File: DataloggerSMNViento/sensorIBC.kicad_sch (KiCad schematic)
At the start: 2 parts

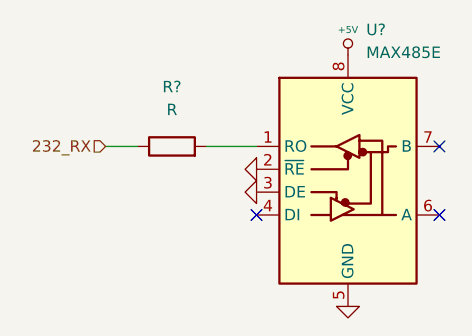
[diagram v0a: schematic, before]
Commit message: Agrego modificaciones al poncho de la EDU CIAA, también agrego una simulacion del circuito para tomar la tensión del ADC del tunnel
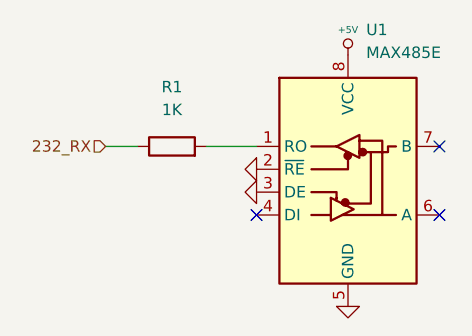
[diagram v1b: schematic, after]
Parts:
- R1: renamed from R?; value R -> 1K; footprint (none) -> Resistor_THT:R_Axial_DIN0207_L6.3mm_D2.5mm_P15.24mm_Horizontal
- U1: renamed from U?; footprint (none) -> Modulos:Rs485toTTL
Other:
- company: (none) -> Servicio Meteorológico Nacional - FIUBA - UBA
- title: (none) -> Datalogger para SCTV
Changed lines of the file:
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@@
 (kicad_sch (version 20211123) (generator eeschema)
   (paper "A4")
+  (title_block
+    (title "Datalogger para SCTV")
+    (date "2023-10-20")
+    (rev "1.0")
+    (company "Servicio Meteorológico Nacional - FIUBA - UBA")
+    (comment 1 "poner repo")
+    (comment 2 "Autores y Licencia del poncho: Cristian Aranda (FIUBA), ver archivo licence.txt")
+    (comment 3 "Autor del poncho: Cristian Zozimo Aranda Cordero.  Ver directorio \"doc\"")
+    (comment 4 "CÓDIGO PONCHO: DT1")
+  )
   (no_connect (at 155.829 67.564))
   (no_connect (at 155.829 75.184))
@@
     (effects (font (size 1.27 1.27)) (justify right))
   )
+  (symbol (lib_id "Device:R") (at 126.111 67.564 90) (unit 1)
+    (in_bom yes) (on_board yes) (fields_autoplaced)
+    (property "Reference" "R1" (id 0) (at 126.111 60.96 90))
+    (property "Value" "1K" (id 1) (at 126.111 63.5 90))
+    (property "Footprint" "Resistor_THT:R_Axial_DIN0207_L6.3mm_D2.5mm_P15.24mm_Horizontal" (id 2) (at 126.111 69.342 90)
+      (effects (font (size 1.27 1.27)) hide)
+    )
+    (property "Datasheet" "~" (id 3) (at 126.111 67.564 0)
+      (effects (font (size 1.27 1.27)) hide)
+    )
+    (pin "1")
+    (pin "2")
+  )
   (symbol (lib_id "Misc_Poncho_Grande:+5V") (at 145.669 57.404 0) (unit 1)
     (in_bom yes) (on_board yes) (fields_autoplaced)
-    (property "Reference" "#PWR?" (id 0) (at 145.669 55.118 0)
+    (property "Reference" "#PWR0103" (id 0) (at 145.669 55.118 0)
       (effects (font (size 0.508 0.508)) hide)
     )
@@
     (pin "1")
   )
-  (symbol (lib_id "Device:R") (at 126.111 67.564 90) (unit 1)
-    (in_bom yes) (on_board yes) (fields_autoplaced)
-    (property "Reference" "R?" (id 0) (at 126.111 60.96 90))
-    (property "Value" "R" (id 1) (at 126.111 63.5 90))
-    (property "Footprint" "" (id 2) (at 126.111 69.342 90)
-      (effects (font (size 1.27 1.27)) hide)
-    )
-    (property "Datasheet" "~" (id 3) (at 126.111 67.564 0)
-      (effects (font (size 1.27 1.27)) hide)
-    )
-    (pin "1")
-    (pin "2")
-  )
   (symbol (lib_id "Misc_Poncho_Grande:GND") (at 135.509 70.104 270) (unit 1)
     (in_bom yes) (on_board yes) (fields_autoplaced)
-    (property "Reference" "#PWR?" (id 0) (at 135.509 70.104 0)
+    (property "Reference" "#PWR01" (id 0) (at 135.509 70.104 0)
       (effects (font (size 0.762 0.762)) hide)
     )
@@
   (symbol (lib_id "Interface_UART:MAX485E") (at 145.669 70.104 0) (unit 1)
     (in_bom yes) (on_board yes) (fields_autoplaced)
-    (property "Reference" "U?" (id 0) (at 147.6884 54.61 0)
+    (property "Reference" "U1" (id 0) (at 147.6884 54.61 0)
       (effects (font (size 1.27 1.27)) (justify left))
     )
@@
       (effects (font (size 1.27 1.27)) (justify left))
     )
-    (property "Footprint" "" (id 2) (at 145.669 87.884 0)
+    (property "Footprint" "Modulos:Rs485toTTL" (id 2) (at 145.669 87.884 0)
       (effects (font (size 1.27 1.27)) hide)
     )
@@
   (symbol (lib_id "Misc_Poncho_Grande:GND") (at 145.669 85.344 0) (unit 1)
     (in_bom yes) (on_board yes) (fields_autoplaced)
-    (property "Reference" "#PWR?" (id 0) (at 145.669 85.344 0)
+    (property "Reference" "#PWR012" (id 0) (at 145.669 85.344 0)
       (effects (font (size 0.762 0.762)) hide)
     )
@@
   (symbol (lib_id "Misc_Poncho_Grande:GND") (at 135.509 72.644 270) (unit 1)
     (in_bom yes) (on_board yes) (fields_autoplaced)
-    (property "Reference" "#PWR?" (id 0) (at 135.509 72.644 0)
+    (property "Reference" "#PWR010" (id 0) (at 135.509 72.644 0)
       (effects (font (size 0.762 0.762)) hide)
     )

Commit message: Subo la version v1.0 del PCB del poncho de la tesis
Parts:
- R1: footprint Resistor_THT:R_Axial_DIN0207_L6.3mm_D2.5mm_P15.24mm_Horizontal -> Resistor_SMD:R_1206_3216Metric
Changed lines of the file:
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@@
     (property "Reference" "R1" (id 0) (at 126.111 60.96 90))
     (property "Value" "1K" (id 1) (at 126.111 63.5 90))
-    (property "Footprint" "Resistor_THT:R_Axial_DIN0207_L6.3mm_D2.5mm_P15.24mm_Horizontal" (id 2) (at 126.111 69.342 90)
+    (property "Footprint" "Resistor_SMD:R_1206_3216Metric" (id 2) (at 126.111 69.342 90)
       (effects (font (size 1.27 1.27)) hide)
     )

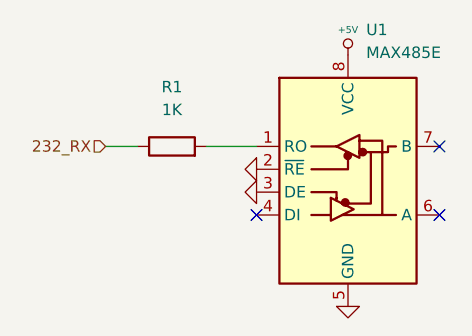
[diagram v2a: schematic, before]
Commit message: Se cambio la alimentacion de los modulos por el stepDown
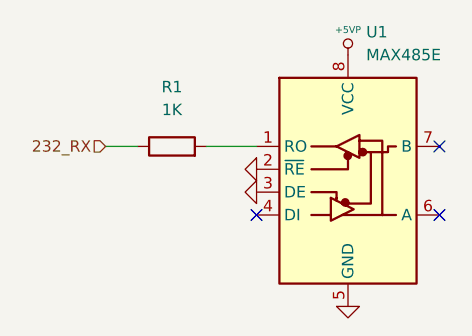
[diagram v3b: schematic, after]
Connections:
- net +5V renamed +5VP
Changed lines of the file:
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@@
     (pin "2")
   )
-  (symbol (lib_id "Misc_Poncho_Grande:+5V") (at 145.669 57.404 0) (unit 1)
+  (symbol (lib_id "Interface_UART:MAX485E") (at 145.669 70.104 0) (unit 1)
     (in_bom yes) (on_board yes) (fields_autoplaced)
-    (property "Reference" "#PWR0103" (id 0) (at 145.669 55.118 0)
-      (effects (font (size 0.508 0.508)) hide)
+    (property "Reference" "U1" (id 0) (at 147.6884 54.864 0)
+      (effects (font (size 1.27 1.27)) (justify left))
     )
-    (property "Value" "+5V" (id 1) (at 145.669 54.61 0)
-      (effects (font (size 0.762 0.762)))
+    (property "Value" "MAX485E" (id 1) (at 147.6884 57.404 0)
+      (effects (font (size 1.27 1.27)) (justify left))
     )
-    (property "Footprint" "" (id 2) (at 145.669 57.404 0)
-      (effects (font (size 1.524 1.524)))
+    (property "Footprint" "Modulos:Rs485toTTL" (id 2) (at 145.669 87.884 0)
+      (effects (font (size 1.27 1.27)) hide)
     )
-    (property "Datasheet" "" (id 3) (at 145.669 57.404 0)
-      (effects (font (size 1.524 1.524)))
+    (property "Datasheet" "https://datasheets.maximintegrated.com/en/ds/MAX1487E-MAX491E.pdf" (id 3) (at 145.669 68.834 0)
+      (effects (font (size 1.27 1.27)) hide)
     )
     (pin "1")
+    (pin "2")
+    (pin "3")
+    (pin "4")
+    (pin "5")
+    (pin "6")
+    (pin "7")
+    (pin "8")
   )
   (symbol (lib_id "Misc_Poncho_Grande:GND") (at 135.509 70.104 270) (unit 1)
@@
     (pin "1")
   )
-  (symbol (lib_id "Interface_UART:MAX485E") (at 145.669 70.104 0) (unit 1)
+  (symbol (lib_id "Misc_Poncho_Grande:+5VP") (at 145.669 57.404 0) (unit 1)
     (in_bom yes) (on_board yes) (fields_autoplaced)
-    (property "Reference" "U1" (id 0) (at 147.6884 54.61 0)
-      (effects (font (size 1.27 1.27)) (justify left))
+    (property "Reference" "#PWR0108" (id 0) (at 145.669 55.118 0)
+      (effects (font (size 0.508 0.508)) hide)
     )
-    (property "Value" "MAX485E" (id 1) (at 147.6884 57.15 0)
-      (effects (font (size 1.27 1.27)) (justify left))
+    (property "Value" "+5VP" (id 1) (at 145.669 54.61 0)
+      (effects (font (size 0.762 0.762)))
     )
-    (property "Footprint" "Modulos:Rs485toTTL" (id 2) (at 145.669 87.884 0)
-      (effects (font (size 1.27 1.27)) hide)
+    (property "Footprint" "" (id 2) (at 145.669 57.404 0)
+      (effects (font (size 1.524 1.524)))
     )
-    (property "Datasheet" "https://datasheets.maximintegrated.com/en/ds/MAX1487E-MAX491E.pdf" (id 3) (at 145.669 68.834 0)
-      (effects (font (size 1.27 1.27)) hide)
+    (property "Datasheet" "" (id 3) (at 145.669 57.404 0)
+      (effects (font (size 1.524 1.524)))
     )
     (pin "1")
-    (pin "2")
-    (pin "3")
-    (pin "4")
-    (pin "5")
-    (pin "6")
-    (pin "7")
-    (pin "8")
   )
   (symbol (lib_id "Misc_Poncho_Grande:GND") (at 145.669 85.344 0) (unit 1)
